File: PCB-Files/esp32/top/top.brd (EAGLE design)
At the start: 50 x 31 mm, 9 parts

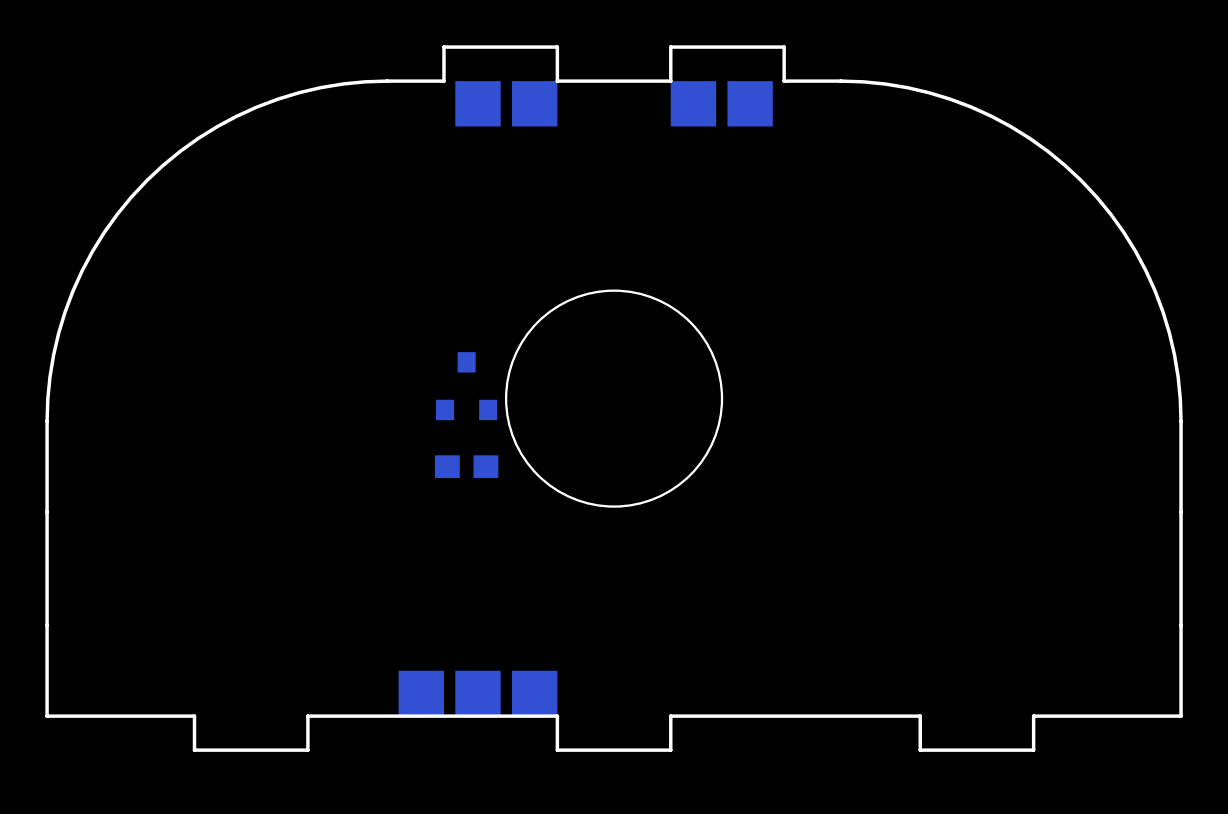
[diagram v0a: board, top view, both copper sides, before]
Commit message: basic layout; dimension for toothed joints
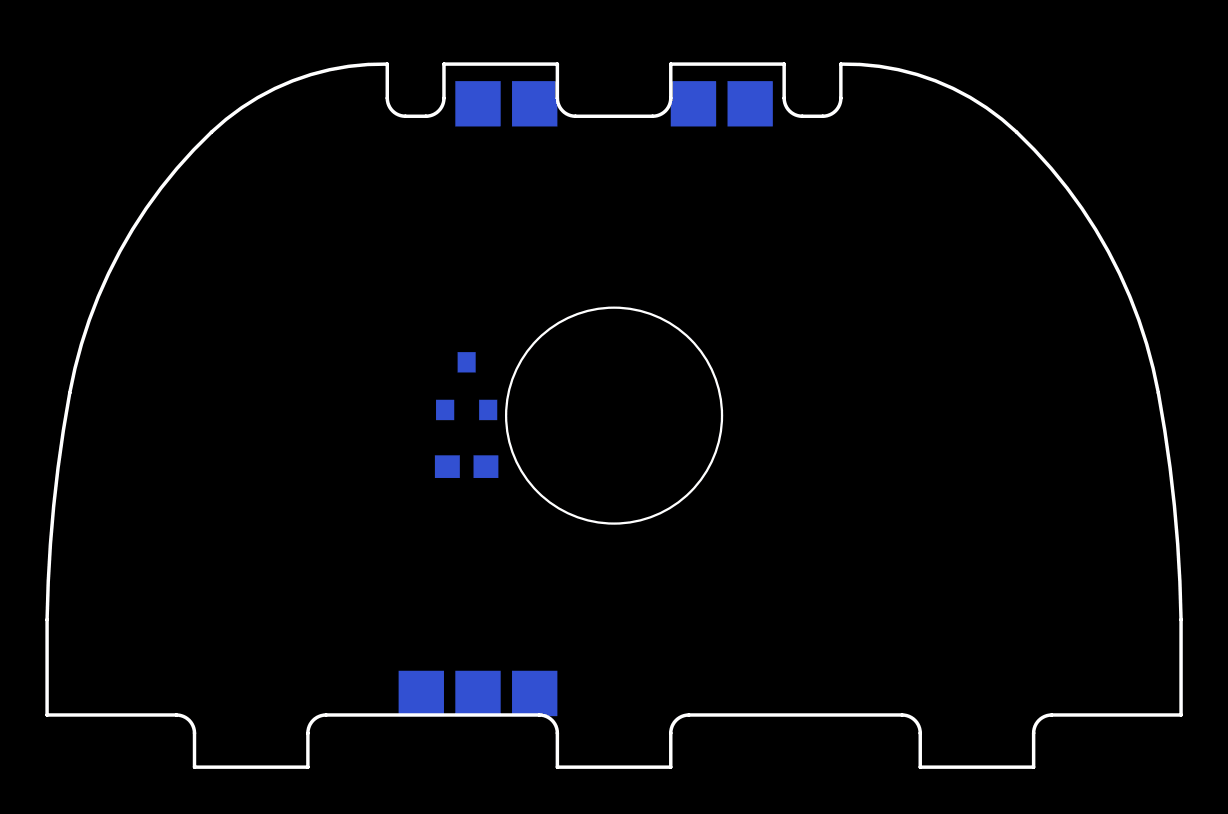
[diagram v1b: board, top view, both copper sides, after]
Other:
- outline, holes or cut-outs redrawn
